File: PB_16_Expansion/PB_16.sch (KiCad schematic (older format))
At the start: 24 parts, among them J1 USB, J2 OLED Conn, J3 GPIO Header, J4 RTC Conn, J5 Power In, J6 VIN_Voltage, J7 Output Header, J8 Output Header, SW1 OLED Select, SW4 Enter BTN, SW5 Down BTN, U1 LM7805, U4 24LC256

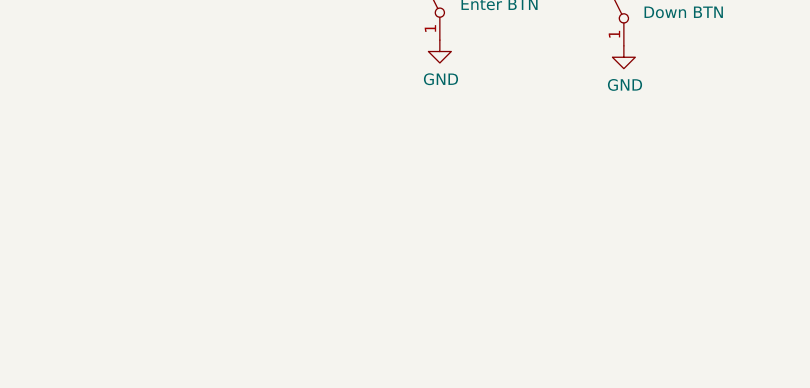
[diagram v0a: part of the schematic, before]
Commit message: added serial header that should work with the E682 Serial PCB
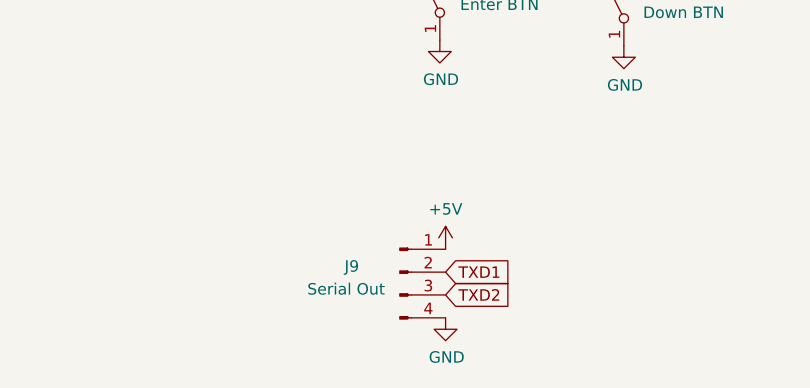
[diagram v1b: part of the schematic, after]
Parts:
- added J9: Serial Out, Connector_PinHeader_2.54mm:PinHeader_1x04_P2.54mm_Vertical, symbol Connector:Conn_01x04_Male
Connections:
- net +5V: now also J9.1 (Pin_1)
- net GND: now also J9.4 (Pin_4)
- new net TXD1: J9.2 (Pin_2)
- new net TXD2: J9.3 (Pin_3)
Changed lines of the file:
@@
 Sheet 1 2
 Title "PB 16 Expansion"
-Date "2019-12-31"
-Rev "v1"
+Date "2020-01-02"
+Rev "v2"
 Comp "Scott Hanson"
 Comment1 ""
@@
 F1 "PocketBeagle.sch" 50
 $EndSheet
+$Comp
+L Connector:Conn_01x04_Male J9
+U 1 1 5E0EED5E
+P 4145 5605
+F 0 "J9" H 3935 5630 50  0000 C CNN
+F 1 "Serial Out" H 3910 5530 50  0000 C CNN
+F 2 "Connector_PinHeader_2.54mm:PinHeader_1x04_P2.54mm_Vertical" H 4145 5605 50  0001 C CNN
+F 3 "~" H 4145 5605 50  0001 C CNN
+	1    4145 5605
+	1    0    0    -1
+$EndComp
+$Comp
+L power:+5V #PWR039
+U 1 1 5E0F04D3
+P 4345 5505
+F 0 "#PWR039" H 4345 5355 50  0001 C CNN
+F 1 "+5V" H 4345 5680 50  0000 C CNN
+F 2 "" H 4345 5505 50  0001 C CNN
+F 3 "" H 4345 5505 50  0001 C CNN
+	1    4345 5505
+	1    0    0    -1
+$EndComp
+$Comp
+L power:GND #PWR040
+U 1 1 5E0F2155
+P 4345 5805
+F 0 "#PWR040" H 4345 5555 50  0001 C CNN
+F 1 "GND" H 4350 5632 50  0000 C CNN
+F 2 "" H 4345 5805 50  0001 C CNN
+F 3 "" H 4345 5805 50  0001 C CNN
+	1    4345 5805
+	1    0    0    -1
+$EndComp
+Text GLabel 4345 5605 2    50   Input ~ 0
+TXD1
+Text GLabel 4345 5705 2    50   Input ~ 0
+TXD2
 $EndSCHEMATC

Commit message: added Serial header part numbers
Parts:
- J9: Digi-Key_PN (none) -> 732-5317-ND; MPN (none) -> 61300411121
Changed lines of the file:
@@
 F 2 "Connector_PinHeader_2.54mm:PinHeader_1x04_P2.54mm_Vertical" H 4145 5605 50  0001 C CNN
 F 3 "~" H 4145 5605 50  0001 C CNN
+F 4 "732-5317-ND" H 4145 5605 50  0001 C CNN "Digi-Key_PN"
+F 5 "61300411121" H 4145 5605 50  0001 C CNN "MPN"
 	1    4145 5605
 	1    0    0    -1
